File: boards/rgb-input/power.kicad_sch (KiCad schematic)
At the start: 19 parts, among them J1 Barrel_Jack, U3 XL1509-5.0

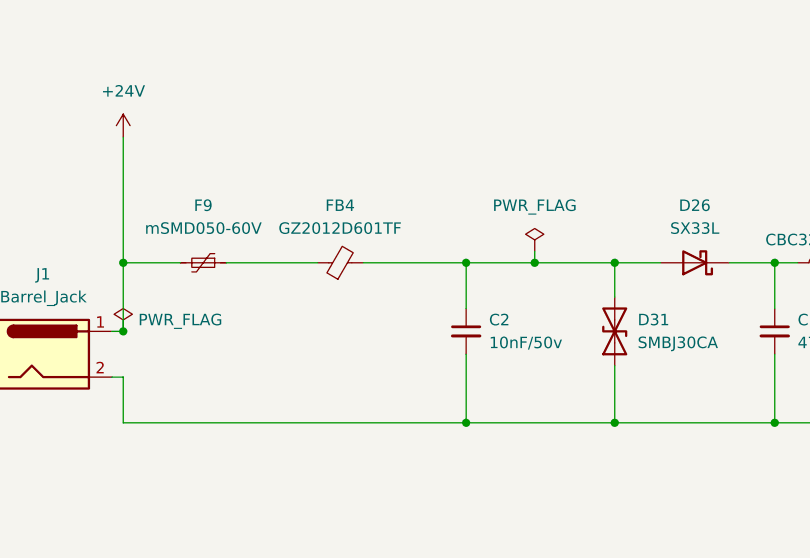
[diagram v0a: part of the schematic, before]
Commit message: first pass on redesign of the rgb input board
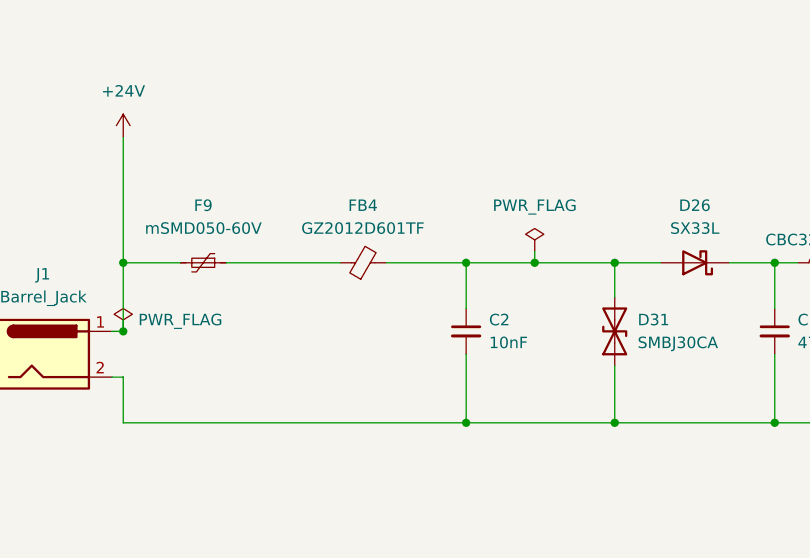
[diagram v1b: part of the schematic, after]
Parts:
- C2: value 10nF/50v -> 10nF
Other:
- moved on the sheet: FB4
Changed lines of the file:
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@@
     (stroke (width 0) (type default))
   )
-  (wire (pts (xy 58.42 80.01) (xy 69.85 80.01))
+  (wire (pts (xy 60.96 80.01) (xy 69.85 80.01))
     (stroke (width 0) (type default))
   )
@@
     (stroke (width 0) (type default))
   )
-  (wire (pts (xy 43.18 80.01) (xy 53.34 80.01))
+  (wire (pts (xy 43.18 80.01) (xy 55.88 80.01))
     (stroke (width 0) (type default))
   )
@@
     )
   )
-  (symbol (lib_id "Device:FerriteBead_Small") (at 55.88 80.01 90) (unit 1)
-    (in_bom yes) (on_board yes) (dnp no) (fields_autoplaced)
-    (property "Reference" "FB4" (at 55.8419 73.66 90)
-      (effects (font (size 1.27 1.27)))
-    )
-    (property "Value" "GZ2012D601TF" (at 55.8419 76.2 90)
-      (effects (font (size 1.27 1.27)))
-    )
-    (property "Footprint" "Inductor_SMD:L_0805_2012Metric" (at 55.88 81.788 90)
-      (effects (font (size 1.27 1.27)) hide)
-    )
-    (property "Datasheet" "~" (at 55.88 80.01 0)
-      (effects (font (size 1.27 1.27)) hide)
-    )
-    (property "LCSC" "C1017" (at 55.88 80.01 90)
+  (symbol (lib_id "Device:FerriteBead_Small") (at 58.42 80.01 90) (unit 1)
+    (in_bom yes) (on_board yes) (dnp no) (fields_autoplaced)
+    (property "Reference" "FB4" (at 58.3819 73.66 90)
+      (effects (font (size 1.27 1.27)))
+    )
+    (property "Value" "GZ2012D601TF" (at 58.3819 76.2 90)
+      (effects (font (size 1.27 1.27)))
+    )
+    (property "Footprint" "Inductor_SMD:L_0805_2012Metric" (at 58.42 81.788 90)
+      (effects (font (size 1.27 1.27)) hide)
+    )
+    (property "Datasheet" "~" (at 58.42 80.01 0)
+      (effects (font (size 1.27 1.27)) hide)
+    )
+    (property "LCSC" "C1017" (at 58.42 80.01 90)
       (effects (font (size 1.27 1.27)) hide)
     )
@@
       (effects (font (size 1.27 1.27)) (justify left))
     )
-    (property "Value" "10nF/50v" (at 72.39 88.9063 0)
-      (effects (font (size 1.27 1.27)) (justify left))
-    )
+    (property "Value" "10nF" (at 72.39 88.9063 0)
+      (effects (font (size 1.27 1.27)) (justify left))
+    )

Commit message: reannotated and did some more cleanup.  almost ready
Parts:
- J3: renamed from J1; symbol Connector:Barrel_Jack -> Connector:Barrel_Jack_Switch
- renumbered F9 to F1, F1 to F2
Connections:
- no-connect marks 0 -> 1
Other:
- company: (none) -> github.com/hoeken/yarrboard
- title: (none) -> RGB Input Board
- moved on the sheet: C1, C2, D26, D31, F1, F2, FB4, L1, L2, R38, U3
